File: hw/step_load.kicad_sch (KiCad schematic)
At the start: 58 parts, among them J1 DC_IN, J2 USB_C_Receptacle_USB2.0_16P, J3 OUTPUT, J4 OLED, J5 UART, J6 BOOT, SW1 RST, SW2 RST, SW3 RST, SW4 RST, U1 AZ1117-3.3, U2 TCA9535PWR, U3 LM35DZ, U4 LM35DZ, U5 ESP32-C3-WROOM-02

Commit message: pcb update
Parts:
- added J7: DC_IN, Connector_PinHeader_2.54mm:PinHeader_1x02_P2.54mm_Vertical, symbol Connector:Conn_01x02_Pin
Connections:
- net +6V: now also J7.1 (Pin_1)
- net GND: now also J7.2 (Pin_2)
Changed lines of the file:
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@@
 	)
 	(junction
+		(at 38.1 168.91)
+		(diameter 0)
+		(color 0 0 0 0)
+	)
+	(junction
 		(at 304.8 30.48)
 		(diameter 0)
@@
 	)
 	(junction
+		(at 35.56 157.48)
+		(diameter 0)
+		(color 0 0 0 0)
+	)
+	(junction
 		(at 361.95 31.75)
 		(diameter 0)
@@
 	(wire
 		(pts
+			(xy 35.56 166.37) (xy 35.56 157.48)
+		)
+		(stroke
+			(width 0)
+			(type default)
+		)
+	)
+	(wire
+		(pts
 			(xy 361.95 31.75) (xy 361.95 38.1)
 		)
@@
 	(wire
 		(pts
+			(xy 38.1 168.91) (xy 38.1 172.72)
+		)
+		(stroke
+			(width 0)
+			(type default)
+		)
+	)
+	(wire
+		(pts
 			(xy 172.72 237.49) (xy 172.72 242.57)
 		)
@@
 	(wire
 		(pts
-			(xy 38.1 157.48) (xy 33.02 157.48)
+			(xy 38.1 157.48) (xy 35.56 157.48)
 		)
 		(stroke
@@
 	(wire
 		(pts
+			(xy 35.56 157.48) (xy 33.02 157.48)
+		)
+		(stroke
+			(width 0)
+			(type default)
+		)
+	)
+	(wire
+		(pts
 			(xy 360.68 127) (xy 358.14 127)
 		)
@@
 	(wire
 		(pts
+			(xy 30.48 168.91) (xy 38.1 168.91)
+		)
+		(stroke
+			(width 0)
+			(type default)
+		)
+	)
+	(wire
+		(pts
 			(xy 304.8 130.81) (xy 304.8 140.97)
 		)
@@
 	(wire
 		(pts
+			(xy 30.48 166.37) (xy 35.56 166.37)
+		)
+		(stroke
+			(width 0)
+			(type default)
+		)
+	)
+	(wire
+		(pts
 			(xy 76.2 24.13) (xy 88.9 24.13)
 		)
@@
 	(symbol
 		(lib_id "power:GND")
-		(at 38.1 168.91 0)
+		(at 38.1 172.72 0)
 		(unit 1)
 		(exclude_from_sim no)
@@
 		(dnp no)
 		(property "Reference" "#PWR07"
-			(at 38.1 175.26 0)
+			(at 38.1 179.07 0)
 			(effects
 				(font
@@
 		)
 		(property "Value" "GND"
-			(at 38.1 172.466 0)
+			(at 38.1 176.276 0)
 			(effects
 				(font
@@
 		)
 		(property "Footprint" ""
-			(at 38.1 168.91 0)
+			(at 38.1 172.72 0)
 			(effects
 				(font
@@
 		)
 		(property "Datasheet" ""
-			(at 38.1 168.91 0)
+			(at 38.1 172.72 0)
 			(effects
 				(font
@@
 		)
 		(property "Description" "Power symbol creates a global label with name \"GND\" , ground"
-			(at 38.1 168.91 0)
+			(at 38.1 172.72 0)
 			(effects
 				(font
@@
 	)
 	(symbol
+		(lib_id "Connector:Conn_01x02_Pin")
+		(at 25.4 166.37 0)
+		(unit 1)
+		(exclude_from_sim no)
+		(in_bom yes)
+		(on_board yes)
+		(dnp no)
+		(property "Reference" "J7"
+			(at 24.13 166.3699 0)
+			(effects
+				(font
+					(size 1.27 1.27)
+				)
+				(justify right)
+			)
+		)
+		(property "Value" "DC_IN"
+			(at 24.13 168.9099 0)
+			(effects
+				(font
+					(size 1.27 1.27)
+				)
+				(justify right)
+			)
+		)
+		(property "Footprint" "Connector_PinHeader_2.54mm:PinHeader_1x02_P2.54mm_Vertical"
+			(at 25.4 166.37 0)
+			(effects
+				(font
+					(size 1.27 1.27)
+				)
+				(hide yes)
+			)
+		)
+		(property "Datasheet" "~"
+			(at 25.4 166.37 0)
+			(effects
+				(font
+					(size 1.27 1.27)
+				)
+				(hide yes)
+			)
+		)
+		(property "Description" "Generic connector, single row, 01x02, script generated"
+			(at 25.4 166.37 0)
+			(effects
+				(font
+					(size 1.27 1.27)
+				)
+				(hide yes)
+			)
+		)
+		(pin "1"
+		)
+		(pin "2"
+		)
+		(instances
+			(project "step_load"
+				(path "/603eb7a1-c3a5-4870-b8f2-de3ec082ba62"
+					(reference "J7")
+					(unit 1)
+				)
+			)
+		)
+	)
+	(symbol
 		(lib_id "Device:R")
 		(at 38.1 210.82 0)
@@
 		)
 		(instances
-			(project "load_resistor"
+			(project "step_load"
 				(path "/603eb7a1-c3a5-4870-b8f2-de3ec082ba62"
 					(page "2")

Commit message: sch & pcb update
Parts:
- added D38: B3V6, Diode_SMD:D_SOD-523, symbol Device:D_Zener
- added R77, R78: 10, Resistor_SMD:R_0603_1608Metric, symbol Device:R
- R2, R3, R7, R9: jlc_part (none) -> C23186; mfr_part (none) -> 0603WAF5101T5E
- R4, R5: jlc_part C118155 -> C21190; mfr_part ERJ3EKF1001V -> 0603WAF1001T5E
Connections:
- net +3.3V: now also D38.1 (K), R78.2; no longer D5.1 (K)
- net GND: now also D38.2 (A)
- new net: D5.1 (K), R77.1
- new net: R77.2, R78.1
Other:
- moved on the sheet: C14, C15, D5, J5, R7, R9, U5

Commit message: pcb update
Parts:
- renumbered C7 to C1, C20 to C10, C14 to C11, C15 to C12, C1 to C13, C2 to C14, C5 to C15, C8 to C16, C9 to C17, C3 to C18, C6 to C19, C10 to C2, C4 to C20, C11 to C3, C12 to C4, C13 to C5, C16 to C6, C17 to C7, C18 to C8, C19 to C9, D3 to D1, D4 to D2, D5 to D3, D38 to D4, D1 to D5, D2 to D6, H3 to H2, H2 to H3, J6 to J1, J5 to J3, J1 to J4, J7 to J5, J4 to J6, J3 to J7, R6 to R17, R8 to R18, R10 to R19, R11 to R20, R12 to R21, R2 to R22, R3 to R23, R4 to R24, R5 to R25, R78 to R26, R77 to R27, R7 to R28, R9 to R29, R1 to R30, U3 to U1, U4 to U2, U1 to U3, U5 to U4, U2 to U5

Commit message: pcb update
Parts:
- C1, C10, C11, C15, C17, C19, C2, C6, C7, C8, C9: jlc_part (none) -> C15849; mfr_part (none) -> CL10A105KB8NNNC
- C13, C14, C16, C18: jlc_part (none) -> C7171; mfr_part (none) -> TAJA106K016RNJ
- D1, D2: jlc_part C2986060 -> C2286; mfr_part 19-217/R6C-AL1M2VY/6T -> KT-0603R
- D3: jlc_part (none) -> C146335; mfr_part (none) -> CUS10S30,H3F
- D4: jlc_part (none) -> C455026; mfr_part (none) -> BZX585-B3V6,115; now not fitted; now left out of the parts list
- D5, D6: footprint Diode_SMD:D_SOD-323_HandSoldering -> Diode_SMD:D_SOD-323
- H1, H2, H3, H4, J4, J6, J7: now not fitted
- J1, J3, J5, NT1, NT2, SW1, SW2, SW3, SW4, U1, U2: now not fitted; now left out of the parts list
- J2: jlc_part C2927039 -> C165948; mfr_part USB-TYPE-C-019 -> TYPE-C-31-M-12
- U3: jlc_part (none) -> C92102
- U4: jlc_part (none) -> C2934560; mfr_part (none) -> ESP32-C3-WROOM-02-N4

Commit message: pcb completed
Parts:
- added R79, R80, R81, R82, R83, R84: 1K, Resistor_SMD:R_0603_1608Metric, symbol Device:R
- U3: now not fitted; now left out of the parts list
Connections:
- net +3.3V: no longer C4.1, C5.1, U1.1 (V+), U2.1 (V+)
- net GND: now also R81.1, R84.1
- net TEMP_AMB: now also R79.1, R80.2; no longer U1.2 (Signal)
- net TEMP_RES: now also R82.1, R83.2; no longer U2.2 (Signal)
- net VIN: now also C4.1, C5.1, U1.1 (V+), U2.1 (V+)
- new net: R83.1, R84.2
- new net: R79.2, U1.2 (Signal)
- new net: R80.1, R81.2
- new net: R82.2, U2.2 (Signal)
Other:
- moved on the sheet: C11, C12, C5, D1, D2, R24, R25, R28, R29, U2, U4

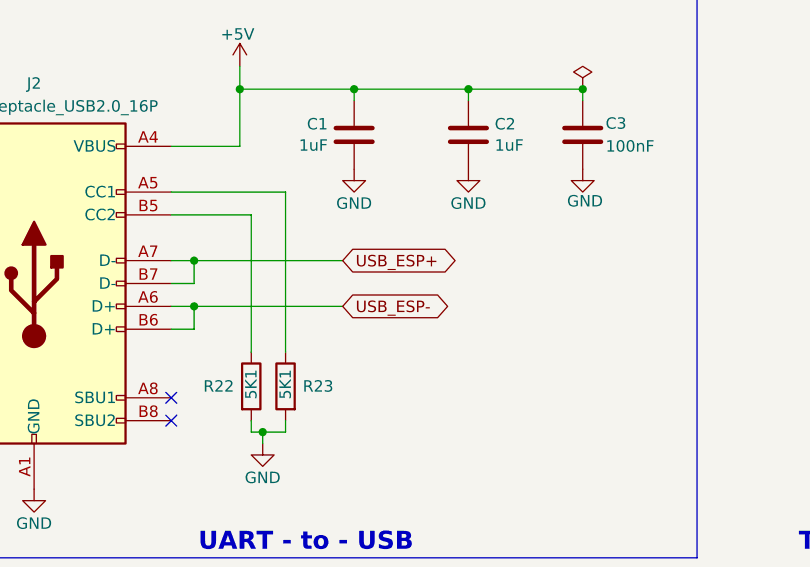
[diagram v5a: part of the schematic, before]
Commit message: Swapt USB+ (A6 & B6) and USB- (A7 & B7) connection, fix the Device Unknown issue
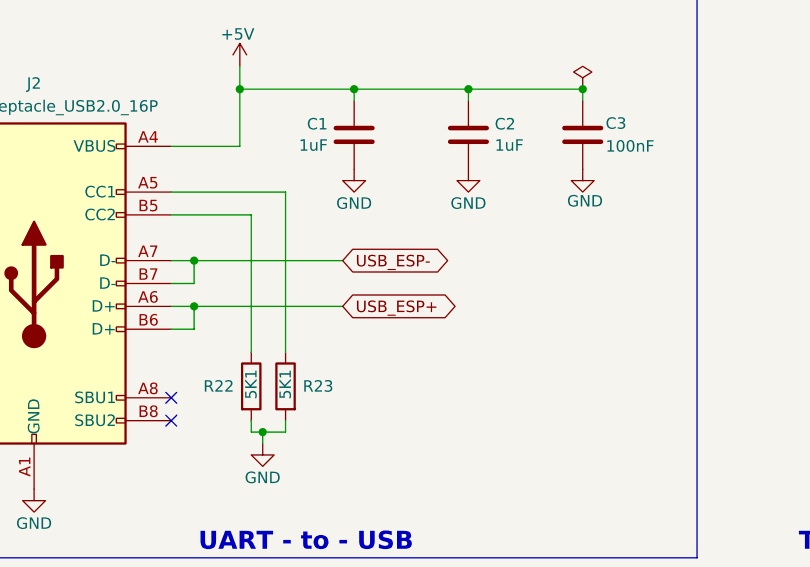
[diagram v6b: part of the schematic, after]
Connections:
- net USB_ESP+: now also J2.A6 (D+), J2.B6 (D+); no longer J2.A7 (D-), J2.B7 (D-)
- net USB_ESP-: now also J2.A7 (D-), J2.B7 (D-); no longer J2.A6 (D+), J2.B6 (D+)
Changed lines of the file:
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@@
 	(global_label "USB_ESP-"
 		(shape bidirectional)
-		(at 62.23 48.26 0)
+		(at 62.23 43.18 0)
 		(fields_autoplaced yes)
 		(effects
@@
 		)
 		(property "Intersheetrefs" "${INTERSHEET_REFS}"
-			(at 76.305 48.26 0)
+			(at 76.305 43.18 0)
 			(effects
 				(font
@@
 	(global_label "USB_ESP+"
 		(shape bidirectional)
-		(at 62.23 43.18 0)
+		(at 62.23 48.26 0)
 		(fields_autoplaced yes)
 		(effects
@@
 		)
 		(property "Intersheetrefs" "${INTERSHEET_REFS}"
-			(at 76.305 43.18 0)
+			(at 76.305 48.26 0)
 			(effects
 				(font
